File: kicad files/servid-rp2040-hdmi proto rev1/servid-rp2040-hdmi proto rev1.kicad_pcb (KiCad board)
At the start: 2 copper layers, 111.8 x 36.8 mm, 81 parts, among them J1 ITU-656, J10 SYNCs, J11 SPKR, J2 INT_LA, J3 I2C_LA, J4 SND_LA, J5 USB_B_Micro-CHECK FOOTPRINT, J6 VIDS, J7 10029449-111RLF-CHANGE FOOTPR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, J8 SWD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

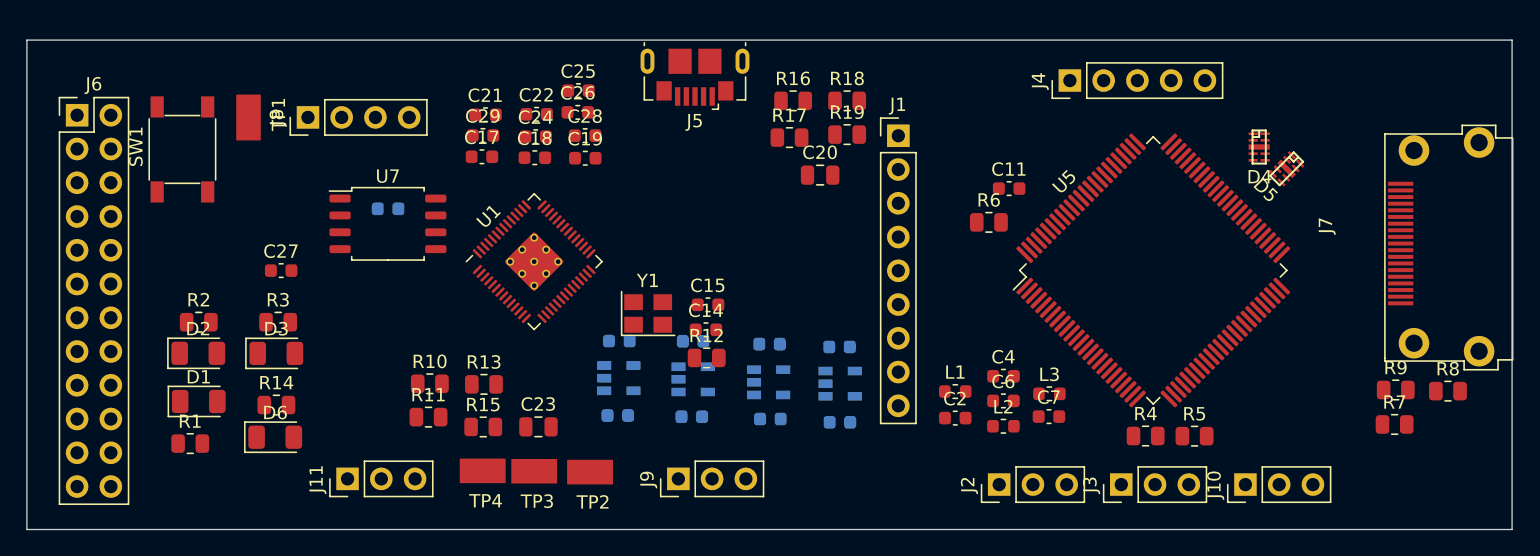
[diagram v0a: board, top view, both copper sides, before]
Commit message: Moved some parts around. consolidating placements and starting to optimize some routes.
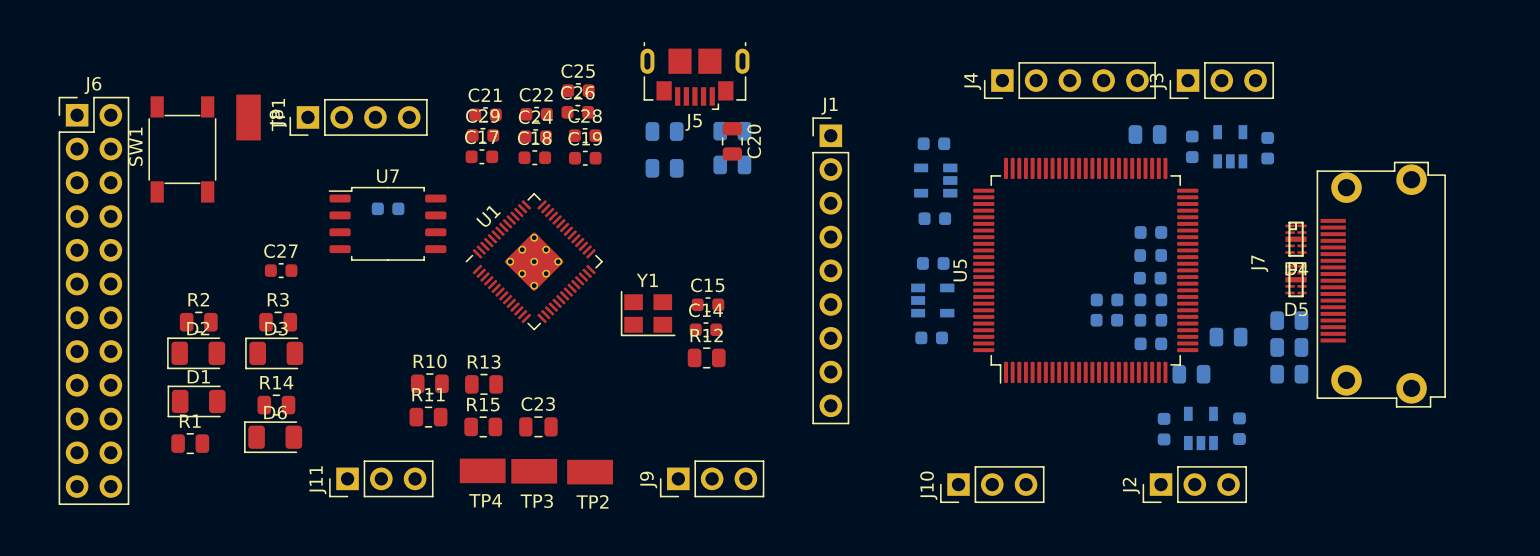
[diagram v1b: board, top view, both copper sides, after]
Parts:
- C11, C2, C4, C6, C7, L1, L2, L3, R16, R17, R18, R19, R4, R5, R6, R7, R8, R9: moved to B.Cu
- moved C8 47.8 mm to (203.9, 127.5), turned to 90 degrees
- moved U3 44.0 mm to (201.0, 127.4), turned to 90 degrees
- moved C5 40.3 mm to (198.2, 127.4), turned to 90 degrees
- moved J3 30.8 mm to (197.9, 122.4)
- moved C13 30.1 mm to (201.7, 148.6), turned to 90 degrees
- moved U6 27.4 mm to (198.8, 148.6), turned to 90 degrees
- moved C12 25.2 mm to (196.1, 148.7), turned to 90 degrees
- moved C1 24.3 mm to (178.7, 136.2)
- moved C3 24.3 mm to (178.6, 141.8)
- moved U2 24.3 mm to (178.7, 139.0)
- moved C9 24.1 mm to (178.7, 127.2), turned to 180 degrees
- moved J10 21.6 mm to (180.6, 152.8)
- moved U4 19.7 mm to (178.9, 130.0), turned to 180 degrees
- moved C2 15.7 mm to (195.1, 142.2), turned to 180 degrees
- moved L1 15.7 mm to (195.1, 140.5)
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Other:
- board outline removed

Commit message: critical routes
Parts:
- removed TP3: TP_SPKR_ADC, My Libraries:Harwin-S1751-46-Test-Point
- added J12: PWR, Connector_PinHeader_2.54mm:PinHeader_1x03_P2.54mm_Vertical, F.Cu at (170.4, 122.4)
- C17, C18, C19, C21, C22, C24, C25, C26, C27, C28, C29, R1, R10, R11, R13, R14, R2, R3: moved to B.Cu
- J1: footprint Connector_PinHeader_2.54mm:PinHeader_1x09_P2.54mm_Vertical -> Connector_PinHeader_2.54mm:PinHeader_2x05_P2.54mm_Vertical
- J11: footprint Connector_PinHeader_2.54mm:PinHeader_1x03_P2.54mm_Vertical -> Connector_PinHeader_2.54mm:PinHeader_1x02_P2.54mm_Vertical
- J4: footprint Connector_PinHeader_2.54mm:PinHeader_1x05_P2.54mm_Vertical -> Connector_PinHeader_2.54mm:PinHeader_1x04_P2.54mm_Vertical
- R12: footprint Resistor_SMD:R_0805_2012Metric -> Resistor_SMD:R_0603_1608Metric
- moved R3 74.7 mm to (203.6, 149.0)
- moved D3 74.0 mm to (203.0, 148.9)
- moved R10 56.5 mm to (195.6, 131.4), turned to 180 degrees
- moved R11 50.9 mm to (189.0, 131.8)
- moved J11 39.8 mm to (160.8, 122.4)
- moved SW1 33.1 mm to (147.7, 148.7), turned to 180 degrees
- moved TP2 28.7 mm to (166.6, 126.7), turned to 90 degrees
- moved R15 28.5 mm to (163.1, 126.6), turned to 270 degrees
- moved TP4 27.9 mm to (157.0, 126.7), turned to 90 degrees
- moved C23 24.9 mm to (160.9, 126.6), turned to 90 degrees
- moved C25 17.7 mm to (151.1, 140.8), turned to 270 degrees
- moved TP1 16.5 mm to (143.5, 127.8), turned to 270 degrees
- moved C27 16.4 mm to (145.0, 131.1), turned to 90 degrees
- moved J1 16.1 mm to (165.6, 141.7), turned to 180 degrees
- moved C22 15.7 mm to (144.7, 140.1), turned to 180 degrees
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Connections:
- net Net-(R13-Pad1) renamed /Run
- J1 pad 1: /CY0 -> /PxCLK
- J1 pad 2: /CY1 -> /CY0
- J1 pad 3: /CY2 -> /CY1
- J1 pad 4: /CY3 -> /CY2
- J1 pad 5: /CY4 -> /CY3
- J1 pad 6: /CY5 -> /CY4
- J1 pad 7: /CY6 -> /CY5
- J1 pad 8: /CY7 -> /CY6
- J1 pad 9: /PxCLK -> /CY7
- J11 pad 2: /SPKR_ADC -> /SPKR_IN
- J4 pad 1: /PIO_I2S_CLK -> /PIO_I2S_WS
- J4 pad 3: /PIO_I2S_WS -> /PIO_I2S_CLK
- J4 pad 4: /SPKR_IN -> GND
- U1 pad 41: /SPKR_ADC -> /SPKR_RC
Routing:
- net /PIO_I2S_CLK: track 0.00 -> 41.5 mm
- net /PIO_I2S_DATA: track 0.00 -> 39.3 mm
- net /PxCLK: track 0.00 -> 38.7 mm, vias 0 -> 1
- net /PIO_I2S_WS: track 0.00 -> 36.6 mm
- net /CY7: track 0.00 -> 33.5 mm
- net /CY6: track 0.00 -> 33.2 mm
- net /CY5: track 0.00 -> 33.0 mm
- net /CY4: track 0.00 -> 32.7 mm
- net /CY3: track 0.00 -> 32.3 mm
- net /CY0: track 0.00 -> 30.6 mm
- net /CY1: track 0.00 -> 29.7 mm
- net /CY2: track 0.00 -> 29.4 mm
- net /14M: track 0.00 -> 23.8 mm
- net /~SYNC: track 0.00 -> 23.3 mm
- net /7M: track 0.00 -> 22.8 mm
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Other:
- board outline added: 88.1 x 34.5 mm
- copper layers 2 -> 4
- net class Default: clearance 0.2 -> 0.1524; trace_width 0.25 -> 0.127; via_dia 0.8 -> 0.4572; via_drill 0.4 -> 0.254
- rule pad_to_mask_clearance: 0 -> 0.0508
- rule trace_clearance: 0.2 -> 0.1524
- rule trace_min: 0.2 -> 0.127
- rule via_min_drill: 0.3 -> 0.254
- rule via_min_size: 0.4 -> 0.4572

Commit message: Power Planes started
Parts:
- moved C10 14.1 mm to (169.5, 141.1), turned to 90 degrees
- moved D6 12.2 mm to (152.6, 150.2)
- moved R1 12.2 mm to (149.5, 149.7)
- moved R14 12.2 mm to (152.6, 149.7)
- moved D1 12.2 mm to (149.4, 150.3)
- moved D2 12.2 mm to (146.3, 150.3)
- moved R2 12.2 mm to (146.3, 149.7)
- moved U4 11.1 mm to (172.2, 141.1), turned to 270 degrees
- moved SW1 10.7 mm to (137.0, 149.6)
- moved R13 10.7 mm to (137.0, 145.7)
- moved C3 9.94 mm to (169.5, 132.2), turned to 90 degrees
- moved C9 8.93 mm to (174.8, 141.1), turned to 270 degrees
- moved U2 6.68 mm to (172.2, 132.3), turned to 270 degrees
- moved C1 4.73 mm to (174.8, 132.3), turned to 270 degrees
- moved R12 1.33 mm to (155.6, 140.3)
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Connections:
- C9 pad 1: +5V -> +3V3
- U4 pad 1: +5V -> +3V3
- U4 pad 3: +5V -> +3V3
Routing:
- net +5V: track 0.00 -> 14.0 mm, vias 0 -> 3
- net /HDMI_5V: track 0.00 -> 9.93 mm, vias 0 -> 1
- net /HPD: track 0.00 -> 7.54 mm, vias 0 -> 1
- net +1V8: track 0.00 -> 5.94 mm, vias 0 -> 4
- net GND: track 0.00 -> 1.30 mm, vias 0 -> 1
- added copper zone on Pwr.Cu, net +1V8
- added copper zone on B.Cu, net +5V
- added copper zone on Pwr.Cu, net +5V
- added copper zone on F.Cu, net /SPKR_IN
- added copper zone on F.Cu, net /SPKR_RC
- added copper zone on F.Cu, net /XIN
- added copper zone on F.Cu, net /XOUT
- added copper zone on F.Cu, net Net-(C15-Pad1)
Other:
- board text added: "1v8"
- board text added: "3v3"
- board text added: "A1v8"
- board text added: "A3v3"
- board text added: "Where are 1v8 caps?"

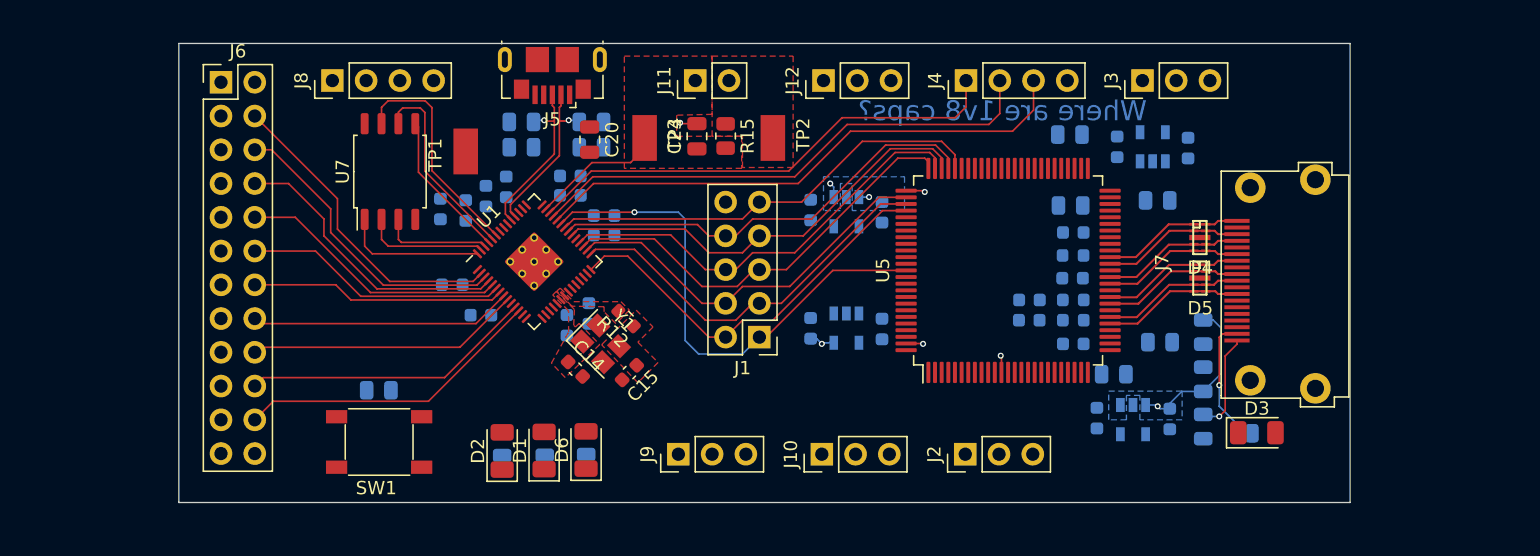
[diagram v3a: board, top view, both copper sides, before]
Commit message: PCB layout Pending review. also need to add titles and graphics.
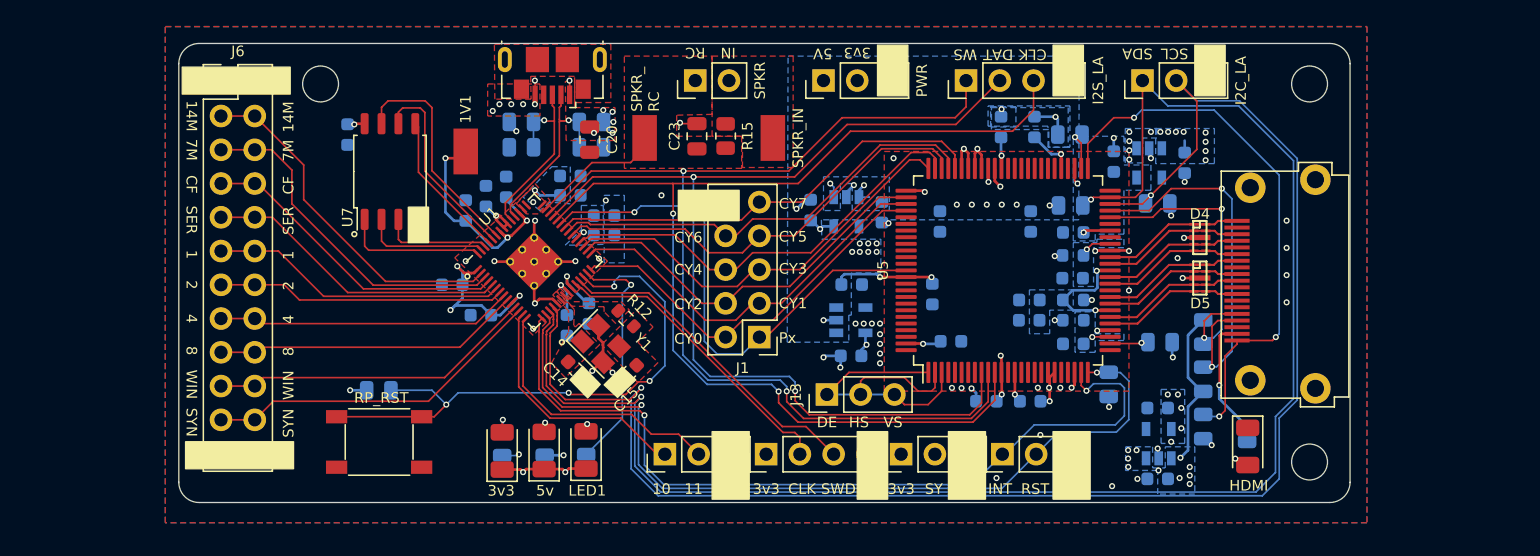
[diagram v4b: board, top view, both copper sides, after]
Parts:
- added C30: 100n, Capacitor_SMD:C_0603_1608Metric, B.Cu at (186.0, 133.0)
- added C31: 100n, Capacitor_SMD:C_0603_1608Metric, B.Cu at (186.3, 125.9)
- added C32: 100n, Capacitor_SMD:C_0603_1608Metric, B.Cu at (183.8, 125.9)
- added C33: 100n, Capacitor_SMD:C_0603_1608Metric, B.Cu at (186.0, 146.6)
- added C34: 100n, Capacitor_SMD:C_0603_1608Metric, B.Cu at (180.0, 142.0)
- added C36: 100n, Capacitor_SMD:C_0603_1608Metric, B.Cu at (182.7, 146.6)
- added C37: 100n, Capacitor_SMD:C_0603_1608Metric, B.Cu at (178.6, 138.5)
- added C38: 100n, Capacitor_SMD:C_0603_1608Metric, B.Cu at (179.2, 133.0)
- added H1: MountingHole, MountingHole:MountingHole_2.7mm_M2.5, F.Cu at (132.6, 122.7)
- added H3: MountingHole, MountingHole:MountingHole_2.7mm_M2.5, F.Cu at (207.0, 122.7)
- added H4: MountingHole, MountingHole:MountingHole_2.7mm_M2.5, F.Cu at (207.0, 151.1)
- added J13: SYNCs, Connector_PinHeader_2.54mm:PinHeader_1x03_P2.54mm_Vertical, F.Cu at (170.7, 146.1)
- J4: value SND_LA -> I2S_LA
- J7: value 10029449-111RLF-CHANGE FOOTPRINT -> 10029449-111RLF
- moved J8 43.1 mm to (166.1, 150.5)
- moved C16 8.95 mm to (134.6, 126.5), turned to 270 degrees
- moved J10 5.97 mm to (176.3, 150.5)
- moved C8 5.68 mm to (192.3, 128.5), turned to 90 degrees
- moved C5 5.22 mm to (197.6, 128.6), turned to 270 degrees
- moved C13 4.64 mm to (195.6, 147.1), turned to 180 degrees
- moved C12 4.60 mm to (195.6, 152.4), turned to 180 degrees
- moved C9 4.05 mm to (172.6, 137.8), turned to 0 degrees
- moved C10 3.67 mm to (172.5, 143.1), turned to 180 degrees
- moved J2 2.79 mm to (183.9, 150.5)
- moved U6 2.65 mm to (195.7, 149.7), turned to 90 degrees
- moved R3 1.98 mm to (202.3, 150.5), turned to 270 degrees
- moved U3 1.24 mm to (194.9, 128.6), turned to 270 degrees
- moved D3 1.24 mm to (202.4, 150.0), turned to 270 degrees
- moved J9 1.02 mm to (158.5, 150.5)
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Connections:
- U5 pad 1: /SYNCs -> /DE
- U5 pad 2: /SYNCs -> /HSYNC
- U5 pad 3: /SYNCs -> /VSYNC
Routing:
- net /I2C_SCL: track 0.00 -> 120.6 mm, vias 0 -> 2
- net /I2C_SDA: track 0.00 -> 120.0 mm, vias 0 -> 2
- net +5V: track 14.0 -> 82.3 mm, vias 3 -> 34
- net /IT_RST#: track 0.00 -> 65.4 mm, vias 0 -> 2
- net /INT#: track 0.00 -> 63.9 mm, vias 0 -> 2
- net GND: track 1.30 -> 62.3 mm, vias 1 -> 59
- net +3V3: track 0.00 -> 47.1 mm, vias 0 -> 32
- net /Run: track 0.00 -> 43.7 mm, vias 0 -> 4
- net /PIO_I2S_CLK: track 41.5 -> 83.8 mm, vias 0 -> 2
- net /PIO_I2S_WS: track 36.6 -> 78.8 mm, vias 0 -> 4
- net /PIO_I2S_DATA: track 39.3 -> 78.4 mm, vias 0 -> 4
- net /HPD: track 7.54 -> 42.2 mm, vias 1 -> 3
- net +1V1: track 0.00 -> 28.8 mm, vias 0 -> 4
- net /DDC_SDA: track 0.00 -> 28.7 mm, vias 0 -> 2
- net Net-(J7-PadSH): track 0.00 -> 24.8 mm
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- added copper zone on B.Cu, net +3V3
- added copper zone on F.Cu, net +3V3
- added copper zone on Pwr.Cu, net +3V3
- added copper zone on F.Cu, net +5V
- added copper zone on B.Cu, net /A1v8
- added copper zone on Pwr.Cu, net /A1v8
- added copper zone on B.Cu, net /A3v3
- added copper zone on B.Cu, net /AVCC18
- added copper zone on B.Cu, net /PVCC1
- added copper zone on B.Cu, net /PVCC2
- added copper zone on B.Cu, net GND
- added copper zone on F.Cu, net GND
- added copper zone on In1.Cu, net GND
- added copper zone on F.Cu, net Net-(J5-Pad6)
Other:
- outline, holes or cut-outs redrawn
- net class Power added: clearance 0.1524, trace_width 0.2032, via_dia 0.4572, via_drill 0.254
- board text added: "0 - Gnd 1 - 3v3 2 - 5v 3 - 1v8"
- board text added: "1"
- board text added: "10"
- board text added: "11"
- board text added: "14M"
- board text added: "1V1"
- board text added: "2"
- board text added: "4"
- board text added: "5V"
- board text added: "7M"
- board text added: "8"
- board text added: "CF"
- board text added: "CLK"
- board text added: "CY0"
- board text added: "CY1"
- board text added: "CY2"
- board text added: "CY3"
- board text added: "CY4"
- board text added: "CY5"
- board text added: "CY6"
- board text added: "CY7"
- board text added: "DAT"
- board text added: "DE"
- board text added: "HS"
- board text added: "IN"
- board text added: "INT"
- board text added: "Px"
- board text added: "RC"
- board text added: "RST"
- board text added: "SCL"
- board text added: "SDA"
- board text added: "SER"
- board text added: "SPKR_ RC"
- board text added: "SPKR_IN"
- board text added: "SWD"
- board text added: "SY"
- board text added: "SYN"
- board text added: "VS"
- board text added: "WIN"
- board text added: "WS"
- board text removed: "Where are 1v8 caps?"

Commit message: rev two board with ibom file
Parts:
- added C35: 1u, Capacitor_SMD:C_0603_1608Metric, B.Cu at (133.0, 136.3)
- added C39: 1u, Capacitor_SMD:C_0603_1608Metric, B.Cu at (137.8, 137.2)
- added JP1: PCADR, Jumper:SolderJumper-2_P1.3mm_Open_TrianglePad1.0x1.5mm, F.Cu at (192.0, 127.8)
- added R20: 470, Resistor_SMD:R_0805_2012Metric, F.Cu at (159.6, 126.6)
- added R21: 1k, Resistor_SMD:R_0805_2012Metric, F.Cu at (157.0, 121.7)
- added R22: 22k, Resistor_SMD:R_0805_2012Metric, F.Cu at (135.9, 144.4)
- added R23: 47k, Resistor_SMD:R_0805_2012Metric, F.Cu at (142.1, 144.0)
- added R24: 22k, Resistor_SMD:R_0805_2012Metric, F.Cu at (146.3, 144.0)
- added R25: 47k, Resistor_SMD:R_0805_2012Metric, F.Cu at (144.3, 144.0)
- added REF**: OSHW-Symbol_6.7x6mm_SilkScreen, Symbol:OSHW-Symbol_6.7x6mm_SilkScreen, B.Cu at (146.9, 144.5)
- added U8: TXB0108PW, Package_SO:TSSOP-20_4.4x6.5mm_P0.65mm, F.Cu at (135.9, 139.7)
- added svg2mod: G***, My Libraries:BE5v2, B.Cu at (139.9, 128.9)
- moved C23 0.89 mm to (161.8, 126.6)
- moved R15 0.89 mm to (164.0, 126.6)
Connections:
- C23 pad 1: /SPKR_RC -> Net-(C23-Pad1)
- R15 pad 2: /SPKR_RC -> Net-(C23-Pad1)
- U1 pad 11: /~WINDOW -> /~bWINDOW
- U1 pad 12: /~SYNC -> /~bSYNC
- U1 pad 2: /14M -> /b14M
- U1 pad 28: /CY0 -> /PxCLK
- U1 pad 29: /CY1 -> /CY0
- U1 pad 3: /7M -> /b7M
- U1 pad 30: /CY2 -> /CY1
- U1 pad 31: /CY3 -> /CY2
- U1 pad 32: /CY4 -> /CY3
- U1 pad 34: /CY5 -> /CY4
- U1 pad 35: /CY6 -> /CY5
- U1 pad 36: /CY7 -> /CY6
- U1 pad 37: /PxCLK -> /CY7
- U1 pad 4: /CREF -> /bCREF
- U1 pad 5: /SERVID -> /bSERVID
- U1 pad 6: /RGB1 -> /bRGB1
- U1 pad 7: /RGB2 -> /bRGB2
- U1 pad 8: /RGB4 -> /bRGB4
- U1 pad 9: /RGB8 -> /bRGB8
- U5 pad 50: Net-(U5-Pad50) -> /PCADR
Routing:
- net +5V: track 82.3 -> 110.7 mm, vias 34 -> 35
- net /RGB8: track 23.2 -> 8.31 mm
- net /~WINDOW: track 24.6 -> 10.3 mm
- net /RGB4: track 22.3 -> 8.34 mm
- net /RGB2: track 21.7 -> 9.13 mm
- net /RGB1: track 22.4 -> 9.91 mm
- net /~bWINDOW: track 0.00 -> 12.5 mm
- net /SERVID: track 23.0 -> 11.9 mm
- net /PxCLK: track 39.3 -> 29.0 mm, vias 1 -> 0
- net /7M: track 25.8 -> 15.6 mm
- net /14M: track 26.5 -> 16.5 mm
- net /CREF: track 23.7 -> 13.8 mm
- net /bRGB8: track 0.00 -> 9.21 mm
- net /bRGB4: track 0.00 -> 8.81 mm
- net /bRGB2: track 0.00 -> 8.33 mm
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- added copper zone on F.Cu, net Net-(C23-Pad1)
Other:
- board text added: "A2 RGB to HDMI 2021-12-07"
- board text added: "Out"
